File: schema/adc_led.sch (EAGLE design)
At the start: 5 parts, among them IC1 PIC16F18875-E_P, IC2 LM50

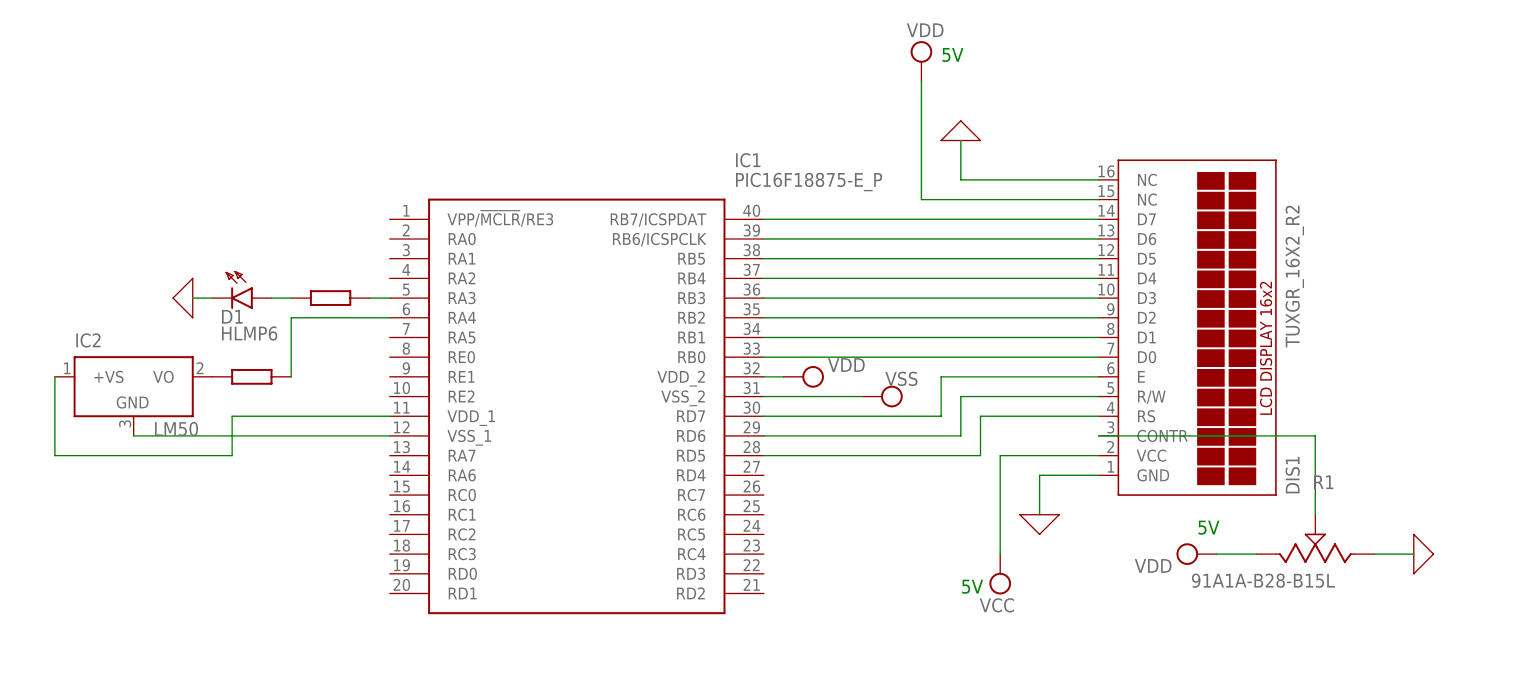
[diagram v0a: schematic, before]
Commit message: update of schema
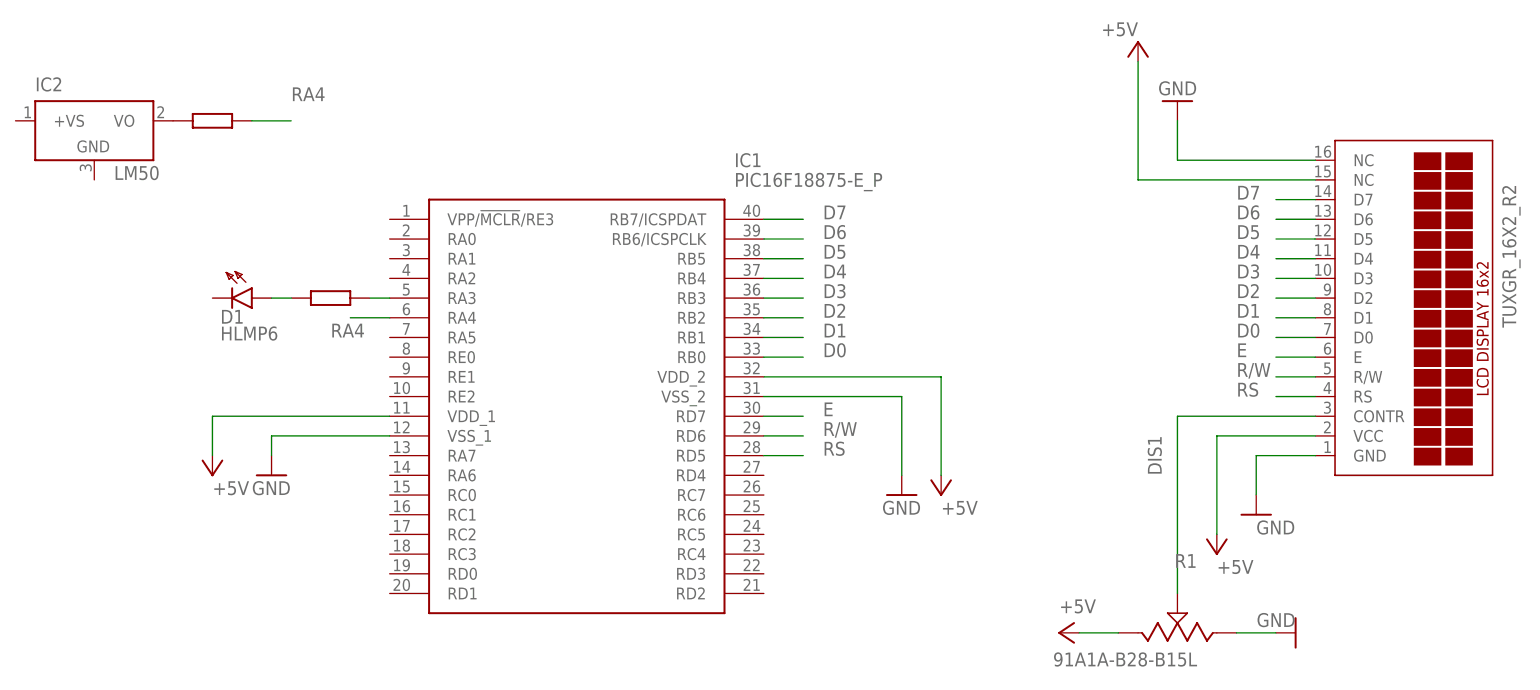
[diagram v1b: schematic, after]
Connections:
- net N$1 renamed D7
- net N$10 renamed R/W
- net N$11 renamed E
- net N$15 renamed RA4
- net N$2 renamed D6
- net N$3 renamed D5
- net N$4 renamed D4
- net N$5 renamed D3
- net N$6 renamed D2
- net N$7 renamed D1
- net N$8 renamed D0
- net N$9 renamed RS
- removed net 0: D1.K, DIS1.GND, DIS1.NC@2, R1.3
- removed net N$16: IC1.VSS_1, IC2.GND
- removed net N$17: IC1.VDD_1, IC2.+VS
- removed net VCC: DIS1.VCC
- removed net VDD: DIS1.NC@1, IC1.VDD_2, R1.1
- removed net VSS: IC1.VSS_2
- new net +5V: DIS1.NC@1, DIS1.VCC, IC1.VDD_1, IC1.VDD_2, R1.1
- new net GND: DIS1.GND, DIS1.NC@2, IC1.VSS_1, IC1.VSS_2, R1.3
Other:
- note removed: "5V"
- moved on the sheet: DIS1, IC2, R1
